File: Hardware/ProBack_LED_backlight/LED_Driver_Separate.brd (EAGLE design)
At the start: 15 x 11 mm, 13 parts, among them U1 LT1937ES5

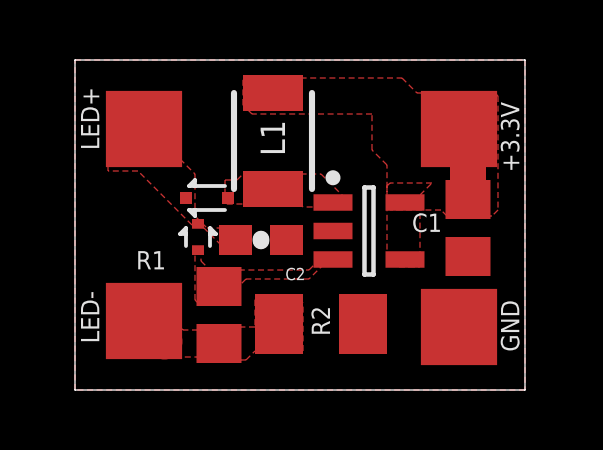
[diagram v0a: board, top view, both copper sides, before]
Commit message: Updated board layout a bit
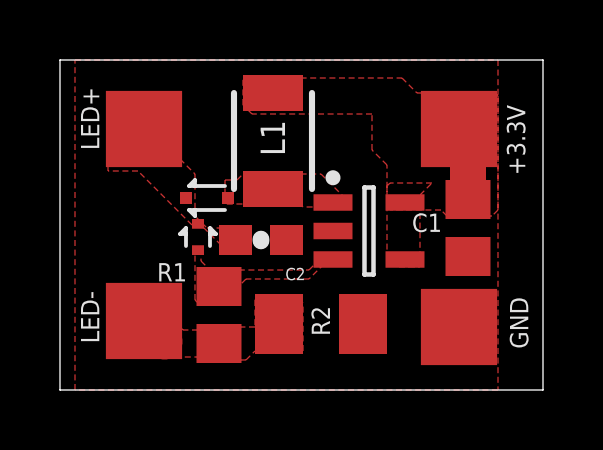
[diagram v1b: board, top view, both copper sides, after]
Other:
- board size 15 x 11 mm -> 16.1 x 11 mm
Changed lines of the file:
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@@
 <layer number="25" name="tNames" color="7" fill="1" visible="yes" active="yes"/>
 <layer number="26" name="bNames" color="7" fill="1" visible="yes" active="yes"/>
-<layer number="27" name="tValues" color="7" fill="1" visible="no" active="yes"/>
+<layer number="27" name="tValues" color="7" fill="1" visible="yes" active="yes"/>
 <layer number="28" name="bValues" color="7" fill="1" visible="no" active="yes"/>
 <layer number="29" name="tStop" color="7" fill="3" visible="no" active="yes"/>
@@
 <board>
 <plain>
-<wire x1="0" y1="0" x2="15" y2="0" width="0" layer="20"/>
-<wire x1="15" y1="0" x2="15" y2="11" width="0" layer="20"/>
-<wire x1="15" y1="11" x2="0" y2="11" width="0" layer="20"/>
-<wire x1="0" y1="11" x2="0" y2="0" width="0" layer="20"/>
+<wire x1="-0.5" y1="0" x2="15.6" y2="0" width="0" layer="20"/>
+<wire x1="15.6" y1="0" x2="15.6" y2="11" width="0" layer="20"/>
+<wire x1="15.6" y1="11" x2="-0.5" y2="11" width="0" layer="20"/>
+<wire x1="-0.5" y1="11" x2="-0.5" y2="0" width="0" layer="20"/>
 </plain>
 <attributes>
@@
 </element>
 <element name="R1" library="Spectron2" package="R0805" value="1K" x="4.8" y="2.5" smashed="yes" rot="R90">
-<attribute name="NAME" x="3.035" y="4.63" size="0.6096" layer="25" rot="R180"/>
+<attribute name="NAME" x="3.735" y="4.23" size="0.6096" layer="25" rot="R180"/>
 <attribute name="VALUE" x="7.34" y="1.865" size="0.8128" layer="27" rot="R90"/>
 </element>
@@
 </element>
 <element name="D1" library="SparkFun-DiscreteSemi" package="SOD-523" value="RB751" x="4.4" y="6.4" smashed="yes" rot="R180">
+<attribute name="LABEL" value="D1" x="3.4" y="7.2" size="0.6096" layer="27" rot="R180"/>
 <attribute name="PROD_ID" value="DIO-11018" x="4.4" y="6.4" size="1.778" layer="27" rot="R180" display="off"/>
 </element>
@@
 </element>
 <element name="+3.3V" library="wirepad" package="SMD2,54-2,54" value="" x="12.8" y="8.7" smashed="yes" rot="R90">
-<attribute name="NAME" x="14.2" y="9.6" size="0.6096" layer="25" rot="R270"/>
+<attribute name="NAME" x="14.4" y="9.5" size="0.6096" layer="25" rot="R270"/>
 <attribute name="VALUE" x="12.8" y="8.7" size="0.0254" layer="27" rot="R90"/>
 </element>
 <element name="GND" library="wirepad" package="SMD2,54-2,54" value="" x="12.8" y="2.1" smashed="yes" rot="R90">
-<attribute name="NAME" x="14.2" y="3" size="0.6096" layer="25" rot="R270"/>
+<attribute name="NAME" x="14.5" y="3.1" size="0.6096" layer="25" rot="R270"/>
 <attribute name="VALUE" x="12.8" y="2.1" size="0.0254" layer="27" rot="R90"/>
 </element>
@@
 <polygon width="0.254" layer="1" thermals="no" rank="6">
 <vertex x="0" y="11"/>
-<vertex x="15" y="11"/>
-<vertex x="15" y="0"/>
+<vertex x="14.1" y="11"/>
+<vertex x="14.1" y="0"/>
 <vertex x="0" y="0"/>
 </polygon>

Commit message: Updated schematic and boards
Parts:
- D2: value DIODE-ZENER -> MM5Z20; device SparkFun-DiscreteSemi:SOD-923 -> SparkFun-DiscreteSemi:SOD-523
- moved D1 0.22 mm to (4.30, 6.60)
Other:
- board text added: "D2"
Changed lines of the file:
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@@
 <wire x1="15.6" y1="11" x2="-0.5" y2="11" width="0" layer="20"/>
 <wire x1="-0.5" y1="11" x2="-0.5" y2="0" width="0" layer="20"/>
+<text x="3.5" y="5.4" size="0.6096" layer="25" rot="R180">D2</text>
 </plain>
 <attributes>
@@
 <attribute name="VALUE" x="5.184" y="3.857" size="0.4064" layer="27" font="vector"/>
 </element>
-<element name="D1" library="SparkFun-DiscreteSemi" package="SOD-523" value="RB751" x="4.4" y="6.4" smashed="yes" rot="R180">
-<attribute name="LABEL" value="D1" x="3.4" y="7.2" size="0.6096" layer="27" rot="R180"/>
-<attribute name="PROD_ID" value="DIO-11018" x="4.4" y="6.4" size="1.778" layer="27" rot="R180" display="off"/>
+<element name="D1" library="SparkFun-DiscreteSemi" package="SOD-523" value="RB751" x="4.3" y="6.6" smashed="yes" rot="R180">
+<attribute name="LABEL" value="D1" x="3.3" y="7.4" size="0.6096" layer="27" rot="R180"/>
+<attribute name="PROD_ID" value="DIO-11018" x="4.3" y="6.6" size="1.778" layer="27" rot="R180" display="off"/>
 </element>
 <element name="U1" library="LT1937ES5" package="LINEAR_TECHNOLOGY_LT1937ES5#TRMPBF_1" value="LT1937ES5" x="9.8" y="5.3" smashed="yes">
@@
 <attribute name="VALUE" x="9.47" y="4.74" size="1.27" layer="27" rot="R180"/>
 </element>
-<element name="D2" library="SparkFun-DiscreteSemi" package="SOD-923" value="DIODE-ZENER" x="4.1" y="5.1" smashed="yes" rot="R90"/>
+<element name="D2" library="SparkFun-DiscreteSemi" package="SOD-523" value="MM5Z20" x="4.1" y="5.1" smashed="yes" rot="R90"/>
 <element name="FRAME1" library="SparkFun-Aesthetics" package="CREATIVE_COMMONS" value="FRAME-LEDGER" x="0" y="0" smashed="yes">
 <attribute name="AUTHOR" value="Alexey Danilchenko" x="0" y="0" size="1.778" layer="27" display="off"/>

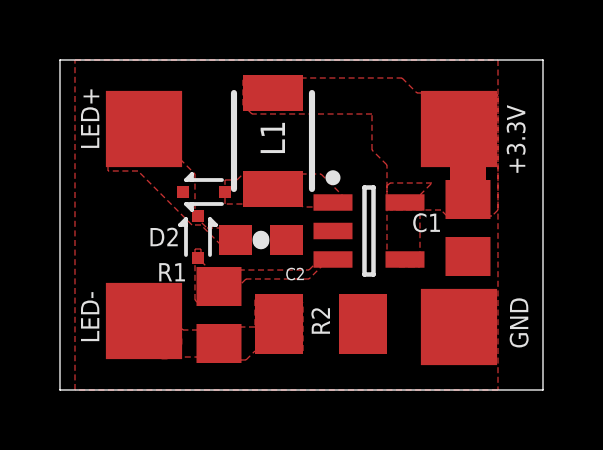
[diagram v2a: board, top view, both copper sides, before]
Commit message: Updated for PCBWay of doing boards
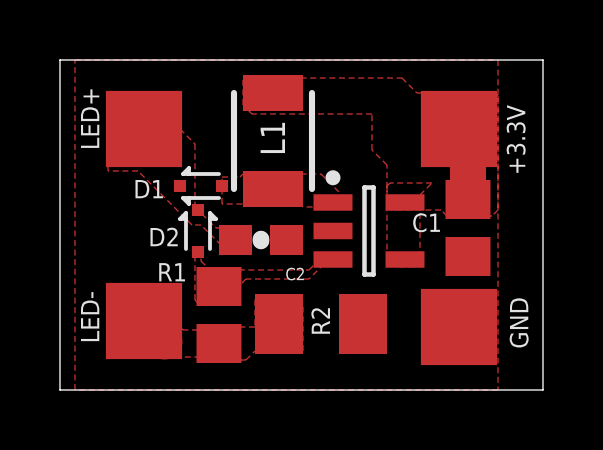
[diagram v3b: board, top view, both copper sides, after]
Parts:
- moved D1 0.22 mm to (4.20, 6.80)
- moved D2 0.20 mm to (4.10, 5.30)
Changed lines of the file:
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@@
 <attribute name="VALUE" x="5.184" y="3.857" size="0.4064" layer="27" font="vector"/>
 </element>
-<element name="D1" library="SparkFun-DiscreteSemi" package="SOD-523" value="RB751" x="4.3" y="6.6" smashed="yes" rot="R180">
-<attribute name="LABEL" value="D1" x="3.3" y="7.4" size="0.6096" layer="27" rot="R180"/>
-<attribute name="PROD_ID" value="DIO-11018" x="4.3" y="6.6" size="1.778" layer="27" rot="R180" display="off"/>
+<element name="D1" library="SparkFun-DiscreteSemi" package="SOD-523" value="RB751" x="4.2" y="6.8" smashed="yes" rot="R180">
+<attribute name="LABEL" value="D1" x="3" y="7" size="0.6096" layer="25" rot="R180"/>
+<attribute name="PROD_ID" value="DIO-11018" x="4.2" y="6.8" size="1.778" layer="27" rot="R180" display="off"/>
 </element>
 <element name="U1" library="LT1937ES5" package="LINEAR_TECHNOLOGY_LT1937ES5#TRMPBF_1" value="LT1937ES5" x="9.8" y="5.3" smashed="yes">
@@
 <attribute name="VALUE" x="9.47" y="4.74" size="1.27" layer="27" rot="R180"/>
 </element>
-<element name="D2" library="SparkFun-DiscreteSemi" package="SOD-523" value="MM5Z20" x="4.1" y="5.1" smashed="yes" rot="R90"/>
+<element name="D2" library="SparkFun-DiscreteSemi" package="SOD-523" value="MM5Z20" x="4.1" y="5.3" smashed="yes" rot="R90"/>
 <element name="FRAME1" library="SparkFun-Aesthetics" package="CREATIVE_COMMONS" value="FRAME-LEDGER" x="0" y="0" smashed="yes">
 <attribute name="AUTHOR" value="Alexey Danilchenko" x="0" y="0" size="1.778" layer="27" display="off"/>
@@
 <contactref element="D1" pad="A"/>
 <polygon width="0.15" layer="1" thermals="no">
-<vertex x="5" y="7"/>
-<vertex x="5.4" y="7"/>
+<vertex x="4.9" y="7.1"/>
+<vertex x="5.5" y="7.1"/>
 <vertex x="5.6" y="7.2"/>
 <vertex x="8.2" y="7.2"/>
@@
 <vertex x="7.6" y="6.1"/>
 <vertex x="7.5" y="6.2"/>
-<vertex x="5" y="6.2"/>
+<vertex x="4.9" y="6.2"/>
 </polygon>
 </signal>
@@
 <vertex x="1.1" y="9.9"/>
 <vertex x="3.5" y="9.9"/>
-<vertex x="3.5" y="7.7"/>
-<vertex x="4" y="7.2"/>
-<vertex x="4" y="5.8"/>
-<vertex x="4.4" y="5.4"/>
+<vertex x="3.5" y="8.7"/>
+<vertex x="4" y="8.2"/>
+<vertex x="4" y="6.1"/>
+<vertex x="4.7" y="5.4"/>
 <vertex x="5.8" y="5.4"/>
 <vertex x="5.8" y="4.6"/>
